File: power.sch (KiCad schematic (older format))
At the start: 20 parts, among them CN400 POWER_CONN, U108 74LS74A, U607 74LS08

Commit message: Fix some DRC fuckery
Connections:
- net +5V: no longer C412.2, C413.2, CN400.13 (Pin_13)
- new net -5V: C412.2, C413.2, CN400.13 (Pin_13)
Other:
- moved on the sheet: D400, D401
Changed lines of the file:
@@
 Connection ~ 2150 1500
-Wire Wire Line
-	2800 1500 3800 1500
 Wire Wire Line
 	3800 1500 3800 1550
@@
 Connection ~ 5250 1500
 Wire Wire Line
-	5900 1500 6400 1500
+	5900 1500 6050 1500
 Connection ~ 5900 1500
 Wire Wire Line
@@
 	2800 1900 2800 1850
 Connection ~ 2150 1900
-Wire Wire Line
-	2800 1900 3800 1900
 Wire Wire Line
 	3800 1900 3800 1850
@@
 	7600 2250 7600 2800
 Connection ~ 7600 2800
-Wire Wire Line
-	2800 2300 8250 2300
 Connection ~ 2800 2300
 Wire Wire Line
-	8250 2300 8250 2150
-Connection ~ 8250 2300
-Wire Wire Line
-	8250 2300 8500 2300
+	8600 2300 8600 2150
+Connection ~ 8600 2300
 $Comp
 L power:+12V #PWR066
 U 1 1 5DE01D08
-P 8250 2150
-F 0 "#PWR066" H 8250 2000 50  0001 C CNN
-F 1 "+12V" H 8265 2323 50  0000 C CNN
-F 2 "" H 8250 2150 50  0001 C CNN
-F 3 "" H 8250 2150 50  0001 C CNN
-	1    8250 2150
+P 8600 2150
+F 0 "#PWR066" H 8600 2000 50  0001 C CNN
+F 1 "+12V" H 8615 2323 50  0000 C CNN
+F 2 "" H 8600 2150 50  0001 C CNN
+F 3 "" H 8600 2150 50  0001 C CNN
+	1    8600 2150
 	1    0    0    -1
 $EndComp
@@
 L Diode:1N4001 D400
 U 1 1 5DE02563
-P 8500 2150
-F 0 "D400" V 8454 2229 50  0000 L CNN
-F 1 "1N4001" V 8545 2229 50  0000 L CNN
-F 2 "Diode_THT:D_DO-41_SOD81_P10.16mm_Horizontal" H 8500 1975 50  0001 C CNN
-F 3 "http://www.vishay.com/docs/88503/1n4001.pdf" H 8500 2150 50  0001 C CNN
-	1    8500 2150
+P 8850 2150
+F 0 "D400" V 8804 2229 50  0000 L CNN
+F 1 "1N4001" V 8895 2229 50  0000 L CNN
+F 2 "Diode_THT:D_DO-41_SOD81_P10.16mm_Horizontal" H 8850 1975 50  0001 C CNN
+F 3 "http://www.vishay.com/docs/88503/1n4001.pdf" H 8850 2150 50  0001 C CNN
+	1    8850 2150
 	0    1    1    0
 $EndComp
-Text GLabel 8500 2000 1    50   Input ~ 0
+Text GLabel 8850 2000 1    50   Input ~ 0
 +12V_USER
 Wire Wire Line
-	4450 2500 9000 2500
+	4450 2500 9250 2500
 $Comp
 L power:-12V #PWR067
 U 1 1 5DE04763
-P 9000 2150
-F 0 "#PWR067" H 9000 2250 50  0001 C CNN
-F 1 "-12V" H 9015 2323 50  0000 C CNN
-F 2 "" H 9000 2150 50  0001 C CNN
-F 3 "" H 9000 2150 50  0001 C CNN
-	1    9000 2150
-	1    0    0    -1
-$EndComp
-Wire Wire Line
-	9000 2150 9000 2500
-Wire Wire Line
-	9000 2500 9250 2500
-Connection ~ 9000 2500
+P 9450 2150
+F 0 "#PWR067" H 9450 2250 50  0001 C CNN
+F 1 "-12V" H 9465 2323 50  0000 C CNN
+F 2 "" H 9450 2150 50  0001 C CNN
+F 3 "" H 9450 2150 50  0001 C CNN
+	1    9450 2150
+	1    0    0    -1
+$EndComp
+Wire Wire Line
+	9450 2150 9450 2500
+Wire Wire Line
+	9450 2500 9650 2500
+Connection ~ 9450 2500
 $Comp
 L Diode:1N4001 D401
 U 1 1 5DE07B85
-P 9250 2150
-F 0 "D401" V 9204 2229 50  0000 L CNN
-F 1 "1N4001" V 9295 2229 50  0000 L CNN
-F 2 "Diode_THT:D_DO-41_SOD81_P10.16mm_Horizontal" H 9250 1975 50  0001 C CNN
-F 3 "http://www.vishay.com/docs/88503/1n4001.pdf" H 9250 2150 50  0001 C CNN
-	1    9250 2150
+P 9650 2150
+F 0 "D401" V 9604 2229 50  0000 L CNN
+F 1 "1N4001" V 9695 2229 50  0000 L CNN
+F 2 "Diode_THT:D_DO-41_SOD81_P10.16mm_Horizontal" H 9650 1975 50  0001 C CNN
+F 3 "http://www.vishay.com/docs/88503/1n4001.pdf" H 9650 2150 50  0001 C CNN
+	1    9650 2150
 	0    1    1    0
 $EndComp
 Wire Wire Line
-	9250 2300 9250 2500
-Text GLabel 9250 2000 1    50   Input ~ 0
+	9650 2300 9650 2500
+Text GLabel 9650 2000 1    50   Input ~ 0
 -12V_USER
-Text GLabel 9800 2000 1    50   Input ~ 0
+Text GLabel 10200 2000 1    50   Input ~ 0
 +5V_USER
-$Comp
-L power:+5V #PWR068
-U 1 1 5DE0B251
-P 10000 2000
-F 0 "#PWR068" H 10000 1850 50  0001 C CNN
-F 1 "+5V" H 10015 2173 50  0000 C CNN
-F 2 "" H 10000 2000 50  0001 C CNN
-F 3 "" H 10000 2000 50  0001 C CNN
-	1    10000 2000
-	1    0    0    -1
-$EndComp
-Text GLabel 10200 2000 1    50   Input ~ 0
+Text GLabel 10800 2000 1    50   Input ~ 0
 TICK
 Wire Wire Line
-	9800 2000 9800 2600
-Wire Wire Line
-	5900 2600 9800 2600
-Wire Wire Line
-	10000 2000 10000 2700
-Wire Wire Line
-	7100 2700 10000 2700
-Wire Wire Line
-	10200 2800 10200 2000
-Wire Wire Line
-	7600 2800 10200 2800
+	10200 2000 10200 2600
+Wire Wire Line
+	5900 2600 10000 2600
+Wire Wire Line
+	10600 2000 10600 2700
+Wire Wire Line
+	7100 2700 10400 2700
+Wire Wire Line
+	10800 2800 10800 2000
+Wire Wire Line
+	7600 2800 10800 2800
 Text Notes 8250 3650 0    50   ~ 0
 SPARES
@@
 	1    0    0    -1
 $EndComp
+$Comp
+L power:PWR_FLAG #FLG0101
+U 1 1 7145FFE0
+P 6050 1500
+F 0 "#FLG0101" H 6050 1575 50  0001 C CNN
+F 1 "PWR_FLAG" H 6050 1673 50  0000 C CNN
+F 2 "" H 6050 1500 50  0001 C CNN
+F 3 "~" H 6050 1500 50  0001 C CNN
+	1    6050 1500
+	1    0    0    -1
+$EndComp
+$Comp
+L power:PWR_FLAG #FLG0102
+U 1 1 71461600
+P 8300 2300
+F 0 "#FLG0102" H 8300 2375 50  0001 C CNN
+F 1 "PWR_FLAG" H 8300 2473 50  0000 C CNN
+F 2 "" H 8300 2300 50  0001 C CNN
+F 3 "~" H 8300 2300 50  0001 C CNN
+	1    8300 2300
+	1    0    0    -1
+$EndComp
+$Comp
+L power:PWR_FLAG #FLG0103
+U 1 1 71461D5D
+P 9250 2500
+F 0 "#FLG0103" H 9250 2575 50  0001 C CNN
+F 1 "PWR_FLAG" H 9250 2673 50  0000 C CNN
+F 2 "" H 9250 2500 50  0001 C CNN
+F 3 "~" H 9250 2500 50  0001 C CNN
+	1    9250 2500
+	1    0    0    -1
+$EndComp
+Connection ~ 9250 2500
+Wire Wire Line
+	9250 2500 9450 2500
+$Comp
+L power:PWR_FLAG #FLG0104
+U 1 1 71462C2B
+P 10000 2600
+F 0 "#FLG0104" H 10000 2675 50  0001 C CNN
+F 1 "PWR_FLAG" H 10000 2773 50  0000 C CNN
+F 2 "" H 10000 2600 50  0001 C CNN
+F 3 "~" H 10000 2600 50  0001 C CNN
+	1    10000 2600
+	1    0    0    -1
+$EndComp
+Connection ~ 10000 2600
+Wire Wire Line
+	10000 2600 10200 2600
+Connection ~ 6050 1500
+Wire Wire Line
+	6050 1500 6400 1500
+$Comp
+L power:-5V #PWR0256
+U 1 1 71463922
+P 10600 2000
+F 0 "#PWR0256" H 10600 2100 50  0001 C CNN
+F 1 "-5V" H 10615 2173 50  0000 C CNN
+F 2 "" H 10600 2000 50  0001 C CNN
+F 3 "" H 10600 2000 50  0001 C CNN
+	1    10600 2000
+	1    0    0    -1
+$EndComp
+Wire Wire Line
+	2800 1500 3800 1500
+$Comp
+L power:PWR_FLAG #FLG0105
+U 1 1 714680F2
+P 10400 2700
+F 0 "#FLG0105" H 10400 2775 50  0001 C CNN
+F 1 "PWR_FLAG" H 10400 2873 50  0000 C CNN
+F 2 "" H 10400 2700 50  0001 C CNN
+F 3 "~" H 10400 2700 50  0001 C CNN
+	1    10400 2700
+	1    0    0    -1
+$EndComp
+Connection ~ 10400 2700
+Wire Wire Line
+	10400 2700 10600 2700
+Connection ~ 8300 2300
+Wire Wire Line
+	8300 2300 8600 2300
+Wire Wire Line
+	2800 2300 8300 2300
+Wire Wire Line
+	2800 1900 3800 1900
+Wire Wire Line
+	8600 2300 8850 2300
 $EndSCHEMATC

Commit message: Fix a bunch of DRC errors
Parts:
- C403, C405: value 0.01uF -> 47uF 16V; symbol Device:C -> Device:CP
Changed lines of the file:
@@
 $EndComp
 $Comp
-L Device:C C403
+L Device:CP C403
 U 1 1 5DDD7BCB
 P 4450 1700
 F 0 "C403" H 4565 1746 50  0000 L CNN
-F 1 "0.01uF" H 4565 1655 50  0000 L CNN
+F 1 "47uF 16V" H 4565 1655 50  0000 L CNN
 F 2 "" H 4488 1550 50  0001 C CNN
 F 3 "~" H 4450 1700 50  0001 C CNN
@@
 $EndComp
 $Comp
-L Device:C C405
+L Device:CP C405
 U 1 1 5DDD87B8
 P 5900 1700
 F 0 "C405" H 6015 1746 50  0000 L CNN
-F 1 "0.01uF" H 6015 1655 50  0000 L CNN
+F 1 "47uF 16V" H 6015 1655 50  0000 L CNN
 F 2 "" H 5938 1550 50  0001 C CNN
 F 3 "~" H 5900 1700 50  0001 C CNN

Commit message: squeak
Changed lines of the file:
@@
 Wire Wire Line
 	8600 2300 8850 2300
+$Comp
+L power:PWR_FLAG #FLG04
+U 1 1 5DA8AE87
+P 6950 1000
+F 0 "#FLG04" H 6950 1075 50  0001 C CNN
+F 1 "PWR_FLAG" H 6950 1173 50  0000 C CNN
+F 2 "" H 6950 1000 50  0001 C CNN
+F 3 "~" H 6950 1000 50  0001 C CNN
+	1    6950 1000
+	1    0    0    -1
+$EndComp
+$Comp
+L power:GND #PWR068
+U 1 1 5DA8B187
+P 6950 1000
+F 0 "#PWR068" H 6950 750 50  0001 C CNN
+F 1 "GND" H 6955 827 50  0000 C CNN
+F 2 "" H 6950 1000 50  0001 C CNN
+F 3 "" H 6950 1000 50  0001 C CNN
+	1    6950 1000
+	1    0    0    -1
+$EndComp
 $EndSCHEMATC

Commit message: Add gender to connectors
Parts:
- CN400: Gender (none) -> Male
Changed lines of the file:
@@
 F 2 "" H 1300 2100 50  0001 C CNN
 F 3 "~" H 1300 2100 50  0001 C CNN
+F 4 "Male" H 1300 2100 50  0001 C CNN "Gender"
 	1    1300 2100
 	1    0    0    -1

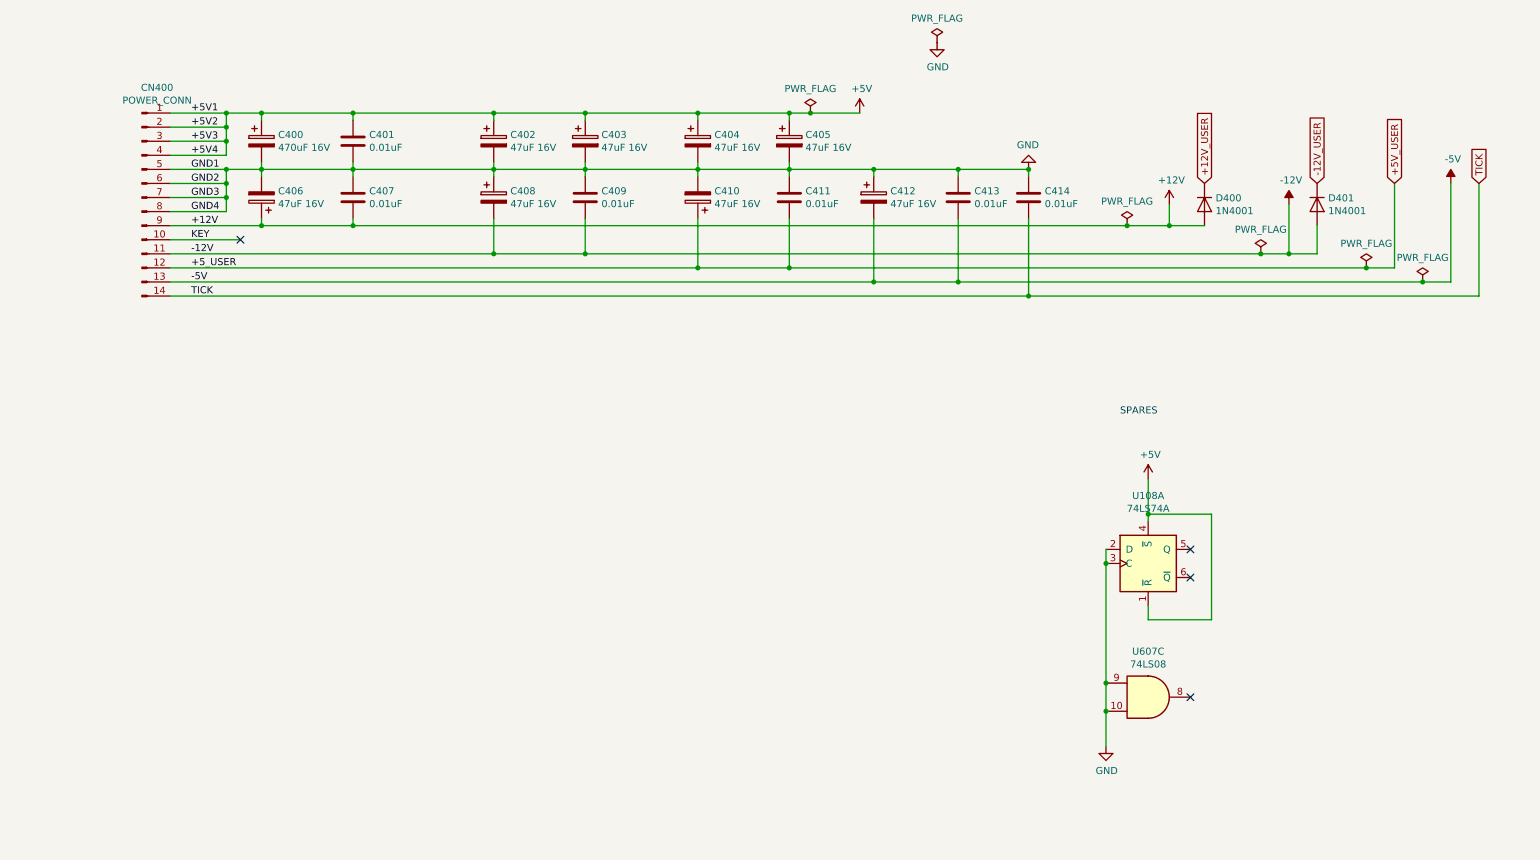
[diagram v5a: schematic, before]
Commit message: Power review; Add missing mouting holes
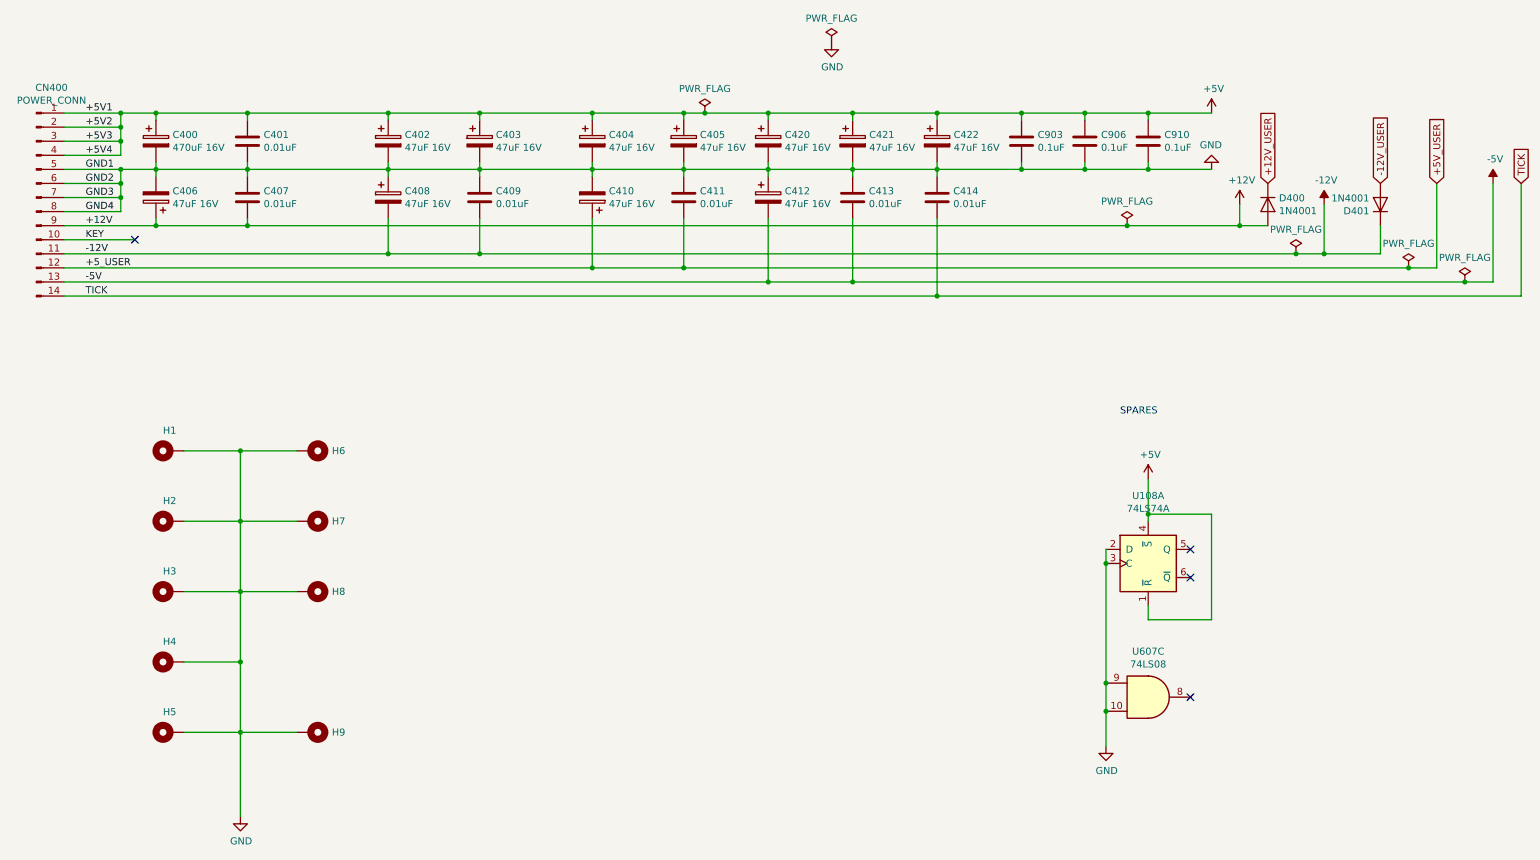
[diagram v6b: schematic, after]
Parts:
- added C420, C421, C422: 47uF 16V, symbol Device:CP
- added C903, C906, C910: 0.1uF, symbol Device:C
- added H1, H2, H3, H4, H5, H6, H7, H8, H9: MountingHole_Pad, symbol Mechanical:MountingHole_Pad
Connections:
- net +5V: now also C420.1, C421.1, C422.1, C903.1, C906.1, C910.1
- net -12V: now also D401.1 (K); no longer D401.2 (A)
- net -12V_USER: now also D401.2 (A); no longer D401.1 (K)
- net GND: now also C420.2, C421.2, C422.2, C903.2, C906.2, C910.2, H1.1, H2.1, H3.1, H4.1, H5.1, H6.1, H7.1, H8.1, H9.1
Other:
- moved on the sheet: C400, C401, C402, C403, C404, C405, C406, C407, C408, C409, C410, C411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

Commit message: Will make next kicad DRC happy
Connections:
- net KEY: no longer names the net of CN400.10 (Pin_10)
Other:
- note added: "key"
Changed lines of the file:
@@
 Text Label 900  2300 0    50   ~ 0
 +12V
-Text Label 900  2400 0    50   ~ 0
-KEY
 Text Label 900  2500 0    50   ~ 0
 -12V
@@
 	1150 2200 1150 2100
 Connection ~ 1150 2100
-Wire Wire Line
-	750  2400 1250 2400
-NoConn ~ 1250 2400
+NoConn ~ 750  2400
 $Comp
 L Device:CP C400
@@
 Wire Wire Line
 	2000 3900 2400 3900
+Text Notes 900  2400 0    50   ~ 0
+key
 $EndSCHEMATC

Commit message: Associate footprints with components
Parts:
- H1, H2, H3, H4, H5, H6, H7, H8, H9: footprint (none) -> MountingHole:MountingHole_4mm_Pad_Via
- U108, U607: footprint (none) -> Package_DIP:DIP-14_W7.62mm_Socket
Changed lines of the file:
@@
 F 0 "U108" H 8450 5181 50  0000 C CNN
 F 1 "74LS74A" H 8450 5090 50  0000 C CNN
-F 2 "" H 8450 4700 50  0001 C CNN
+F 2 "Package_DIP:DIP-14_W7.62mm_Socket" H 8450 4700 50  0001 C CNN
 F 3 "74xx/74hc_hct74.pdf" H 8450 4700 50  0001 C CNN
 	1    8450 4700
@@
 F 0 "U607" H 8450 5975 50  0000 C CNN
 F 1 "74LS08" H 8450 5884 50  0000 C CNN
-F 2 "" H 8450 5650 50  0001 C CNN
+F 2 "Package_DIP:DIP-14_W7.62mm_Socket" H 8450 5650 50  0001 C CNN
 F 3 "http://www.ti.com/lit/gpn/sn74LS08" H 8450 5650 50  0001 C CNN
 	3    8450 5650
@@
 F 0 "H1" V 1645 3903 50  0000 C CNN
 F 1 "MountingHole_Pad" H 1600 3858 50  0001 L CNN
-F 2 "" H 1500 3900 50  0001 C CNN
+F 2 "MountingHole:MountingHole_4mm_Pad_Via" H 1500 3900 50  0001 C CNN
 F 3 "~" H 1500 3900 50  0001 C CNN
 	1    1500 3900
@@
 F 0 "H2" V 1645 4403 50  0000 C CNN
 F 1 "MountingHole_Pad" H 1600 4358 50  0001 L CNN
-F 2 "" H 1500 4400 50  0001 C CNN
+F 2 "MountingHole:MountingHole_4mm_Pad_Via" H 1500 4400 50  0001 C CNN
 F 3 "~" H 1500 4400 50  0001 C CNN
 	1    1500 4400
@@
 F 0 "H3" V 1645 4903 50  0000 C CNN
 F 1 "MountingHole_Pad" H 1600 4858 50  0001 L CNN
-F 2 "" H 1500 4900 50  0001 C CNN
+F 2 "MountingHole:MountingHole_4mm_Pad_Via" H 1500 4900 50  0001 C CNN
 F 3 "~" H 1500 4900 50  0001 C CNN
 	1    1500 4900
@@
 F 0 "H4" V 1645 5403 50  0000 C CNN
 F 1 "MountingHole_Pad" H 1600 5358 50  0001 L CNN
-F 2 "" H 1500 5400 50  0001 C CNN
+F 2 "MountingHole:MountingHole_4mm_Pad_Via" H 1500 5400 50  0001 C CNN
 F 3 "~" H 1500 5400 50  0001 C CNN
 	1    1500 5400
@@
 F 0 "H5" V 1645 5903 50  0000 C CNN
 F 1 "MountingHole_Pad" H 1600 5858 50  0001 L CNN
-F 2 "" H 1500 5900 50  0001 C CNN
+F 2 "MountingHole:MountingHole_4mm_Pad_Via" H 1500 5900 50  0001 C CNN
 F 3 "~" H 1500 5900 50  0001 C CNN
 	1    1500 5900
@@
 F 0 "H6" V 2500 4050 50  0000 L CNN
 F 1 "MountingHole_Pad" H 2600 3858 50  0001 L CNN
-F 2 "" H 2500 3900 50  0001 C CNN
+F 2 "MountingHole:MountingHole_4mm_Pad_Via" H 2500 3900 50  0001 C CNN
 F 3 "~" H 2500 3900 50  0001 C CNN
 	1    2500 3900
@@
 F 0 "H7" V 2500 4550 50  0000 L CNN
 F 1 "MountingHole_Pad" H 2600 4358 50  0001 L CNN
-F 2 "" H 2500 4400 50  0001 C CNN
+F 2 "MountingHole:MountingHole_4mm_Pad_Via" H 2500 4400 50  0001 C CNN
 F 3 "~" H 2500 4400 50  0001 C CNN
 	1    2500 4400
@@
 F 0 "H8" V 2500 5050 50  0000 L CNN
 F 1 "MountingHole_Pad" H 2600 4858 50  0001 L CNN
-F 2 "" H 2500 4900 50  0001 C CNN
+F 2 "MountingHole:MountingHole_4mm_Pad_Via" H 2500 4900 50  0001 C CNN
 F 3 "~" H 2500 4900 50  0001 C CNN
 	1    2500 4900
@@
 F 0 "H9" V 2500 6050 50  0000 L CNN
 F 1 "MountingHole_Pad" H 2600 5858 50  0001 L CNN
-F 2 "" H 2500 5900 50  0001 C CNN
+F 2 "MountingHole:MountingHole_4mm_Pad_Via" H 2500 5900 50  0001 C CNN
 F 3 "~" H 2500 5900 50  0001 C CNN
 	1    2500 5900
